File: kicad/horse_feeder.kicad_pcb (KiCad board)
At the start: 2 copper layers, 100 x 80 mm, 81 parts, among them J1 Screw_Terminal_01x04, J10 Conn_01x04_Male, J2 Screw_Terminal_01x04, J3 Screw_Terminal_01x04, J4 Screw_Terminal_01x04, J5 Screw_Terminal_01x04, J6 Screw_Terminal_01x04, J8 Barrel_Jack_Switch_Pin3Ring, J9 Barrel_Jack_Switch_Pin3Ring, Q1 BSS306NH, Q2 BSS306NH, Q3 BSS306NH, Q4 BSS306NH, Q5 BSS306NH, Q6 BSS306NH, SW1 SW_Push, SW2 SW_Push, SW3 SW_Push, SW4 SW_Push, U1 IX4340NE, U2 IX4340NE, U3 IX4340NE, U4 ESP32DevKitCV4, U5 L7809, U6 L7805

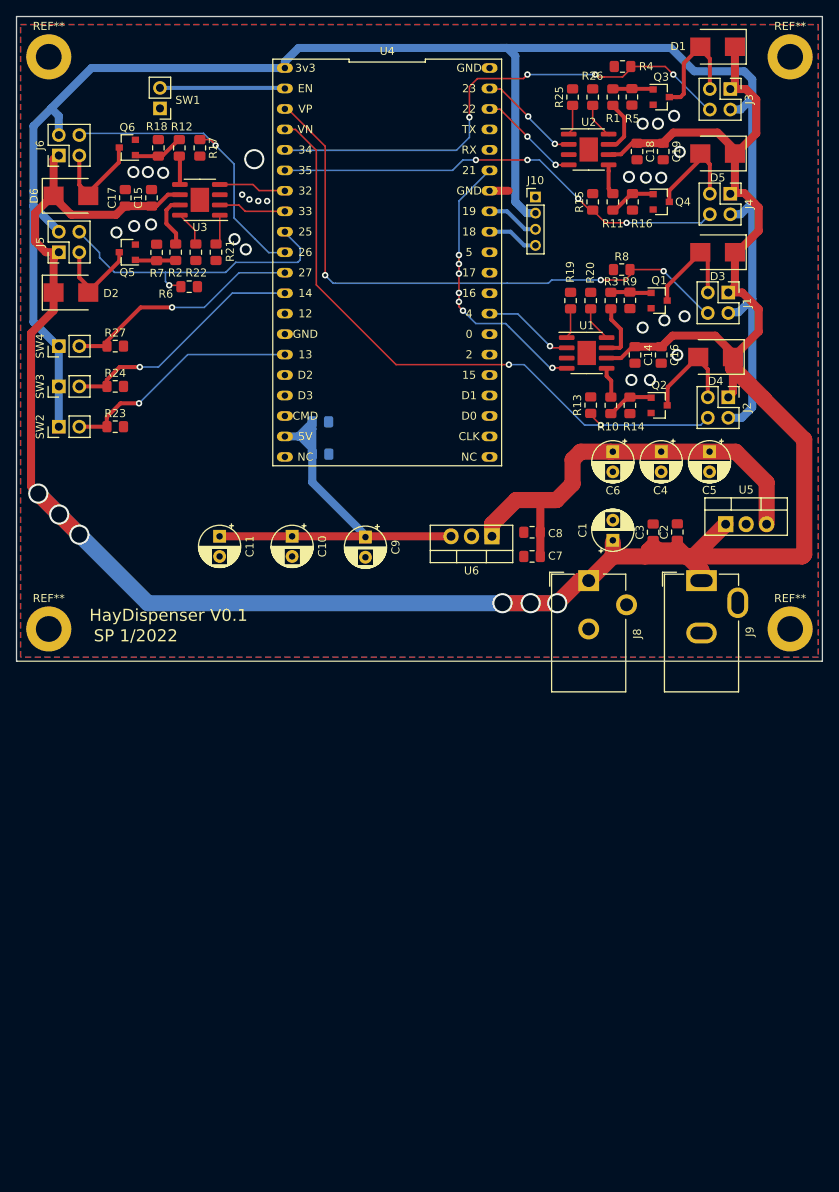
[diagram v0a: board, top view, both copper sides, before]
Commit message: Added pullups for I2C
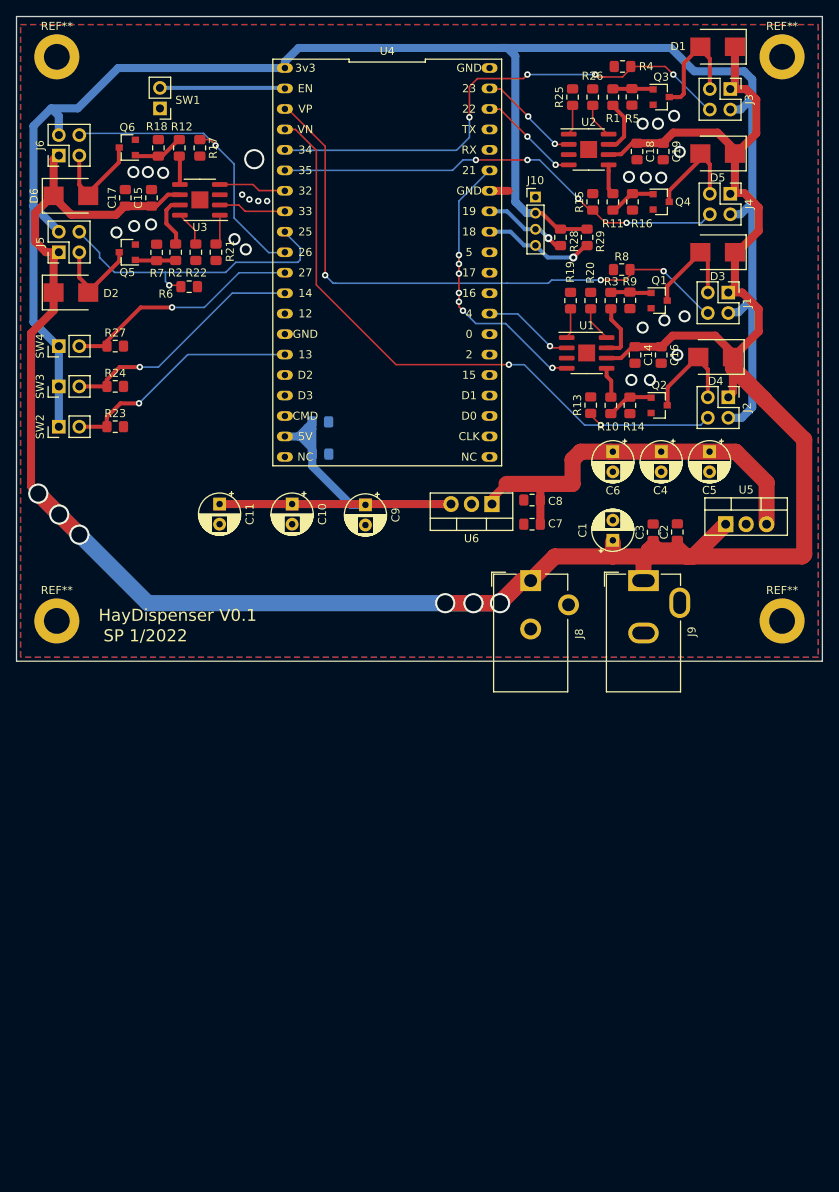
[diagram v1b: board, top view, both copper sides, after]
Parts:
- removed the REF** at (116.0, 45.0)
- removed the REF** at (24.0, 45.0)
- removed the REF** at (24.0, 116.0)
- added R28: 3k3, Resistor_SMD:R_0805_2012Metric_Pad1.15x1.40mm_HandSolder, F.Cu at (87.5, 67.4)
- added R29: 3k3, Resistor_SMD:R_0805_2012Metric_Pad1.15x1.40mm_HandSolder, F.Cu at (90.8, 67.4)
- added REF**: MountingHole_3.2mm_M3_DIN965_Pad, MountingHole:MountingHole_3.2mm_M3_DIN965_Pad, F.Cu at (115.0, 45.0)
- added REF**: MountingHole_3.2mm_M3_DIN965_Pad, MountingHole:MountingHole_3.2mm_M3_DIN965_Pad, F.Cu at (25.0, 45.0)
- added REF**: MountingHole_3.2mm_M3_DIN965_Pad, MountingHole:MountingHole_3.2mm_M3_DIN965_Pad, F.Cu at (25.0, 115.0)
- U1, U2, U3: footprint Package_SO:SOIC-8-1EP_3.9x4.9mm_P1.27mm_EP2.29x3mm -> mosfet_drivers:IX4340NE
- moved J8 7.20 mm to (83.8, 110.0)
- moved J9 7.20 mm to (97.8, 110.0)
- moved C10 4.00 mm to (54.2, 100.5)
- moved C11 4.00 mm to (45.2, 100.5)
- moved C7 4.00 mm to (84.0, 103.0)
- moved C8 4.00 mm to (84.0, 100.0)
- moved C9 4.00 mm to (63.3, 100.6)
- moved U6 4.00 mm to (79.0, 100.5)
- moved REF** 1.41 mm to (115.0, 115.0)
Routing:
- net +12V: track 322.8 -> 334.2 mm
- net /mcu/SCL: track 6.50 -> 14.1 mm, vias 0 -> 1
- net +3V3: track 219.9 -> 227.1 mm
- net /mcu/SDA: track 6.72 -> 10.7 mm, vias 0 -> 1
- net +5V: track 58.2 -> 56.1 mm
- net +9V: track 56.8 -> 58.0 mm

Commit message: KiCAD latest version now up to date
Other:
- net class Default removed
- net class Minimum removed
- net class Power removed
- net class Power2 removed
- net class Signal removed

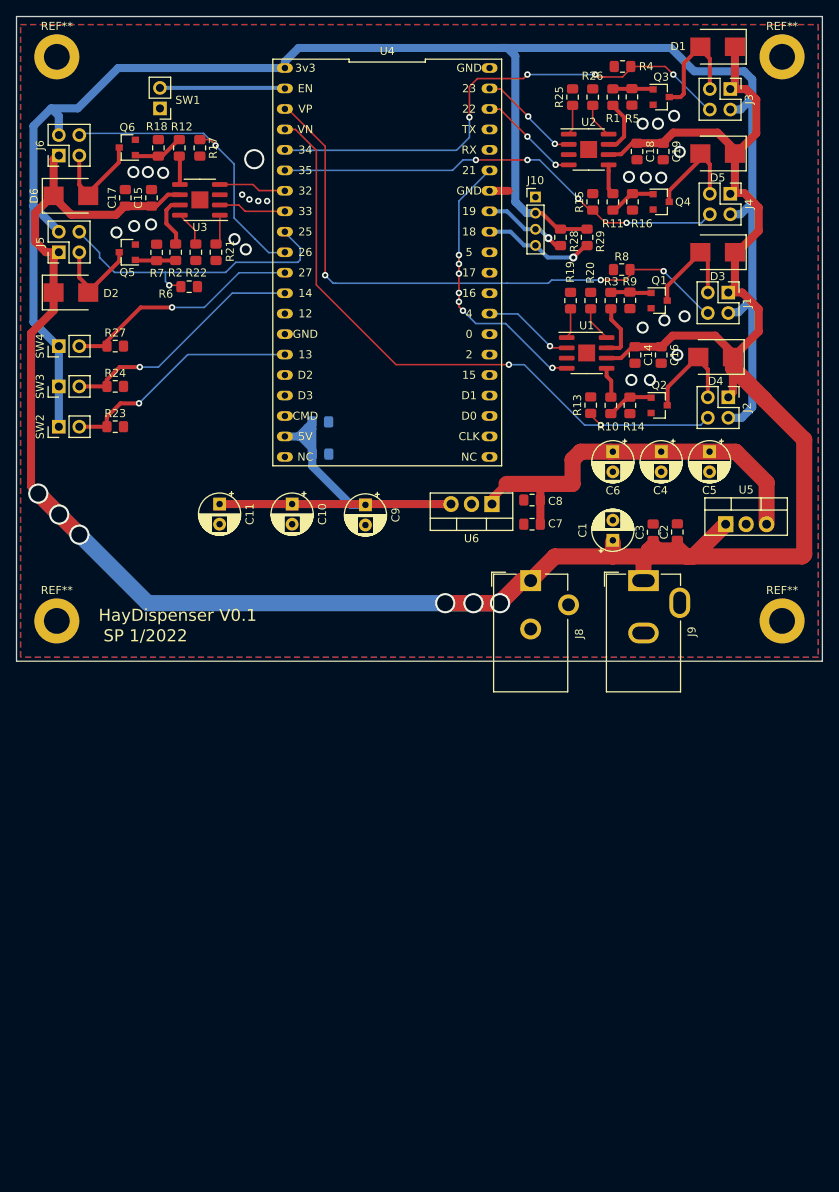
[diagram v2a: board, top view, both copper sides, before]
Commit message: Update PCB with IO expander
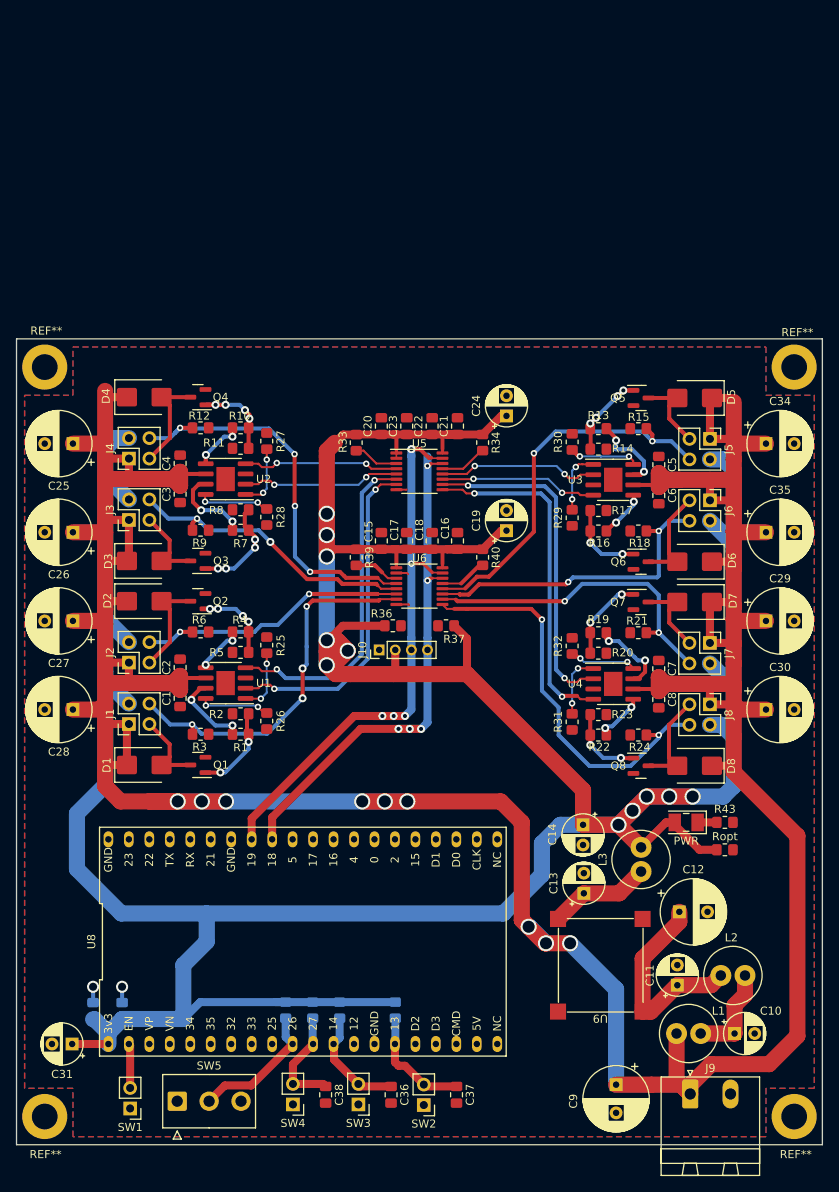
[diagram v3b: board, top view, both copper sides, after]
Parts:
- removed the REF** at (115.0, 115.0)
- removed the REF** at (115.0, 45.0)
- removed the REF** at (25.0, 115.0)
- removed the REF** at (25.0, 45.0)
- added C20: 100p, Capacitor_SMD:C_0805_2012Metric_Pad1.18x1.45mm_HandSolder, F.Cu at (65.3, 90.8)
- added C21: 100p, Capacitor_SMD:C_0805_2012Metric_Pad1.18x1.45mm_HandSolder, F.Cu at (74.7, 90.8)
- added C22: 47n, Capacitor_SMD:C_0805_2012Metric_Pad1.18x1.45mm_HandSolder, F.Cu at (71.6, 90.8)
- added C23: 47n, Capacitor_SMD:C_0805_2012Metric_Pad1.18x1.45mm_HandSolder, F.Cu at (68.4, 90.8)
- added C24: 100u, Capacitor_THT:CP_Radial_D5.0mm_P2.50mm, F.Cu at (80.8, 89.6)
- added C25: 330u, Capacitor_THT:CP_Radial_D8.0mm_P3.50mm, F.Cu at (27.0, 93.0)
- added C26: 330u, Capacitor_THT:CP_Radial_D8.0mm_P3.50mm, F.Cu at (27.0, 104.0)
- added C27: 330u, Capacitor_THT:CP_Radial_D8.0mm_P3.50mm, F.Cu at (27.0, 115.0)
- added C28: 330u, Capacitor_THT:CP_Radial_D8.0mm_P3.50mm, F.Cu at (27.0, 126.0)
- added C29: 330u, Capacitor_THT:CP_Radial_D8.0mm_P3.50mm, F.Cu at (113.0, 115.0)
- added C30: 330u, Capacitor_THT:CP_Radial_D8.0mm_P3.50mm, F.Cu at (113.0, 126.0)
- added C31: 100u, Capacitor_THT:CP_Radial_D5.0mm_P2.50mm, F.Cu at (26.9, 167.5)
- added C32: 47n, Capacitor_SMD:C_0805_2012Metric_Pad1.18x1.45mm_HandSolder, B.Cu at (29.5, 163.4)
- added C33: 100p, Capacitor_SMD:C_0805_2012Metric_Pad1.18x1.45mm_HandSolder, B.Cu at (33.1, 163.4)
- added C34: 330u, Capacitor_THT:CP_Radial_D8.0mm_P3.50mm, F.Cu at (113.0, 93.0)
- added C35: 330u, Capacitor_THT:CP_Radial_D8.0mm_P3.50mm, F.Cu at (113.0, 104.0)
- added C36: 47u, Capacitor_SMD:C_0805_2012Metric_Pad1.18x1.45mm_HandSolder, F.Cu at (66.5, 173.8)
- added C37: 47u, Capacitor_SMD:C_0805_2012Metric_Pad1.18x1.45mm_HandSolder, F.Cu at (74.6, 173.8)
- added C38: 47u, Capacitor_SMD:C_0805_2012Metric_Pad1.18x1.45mm_HandSolder, F.Cu at (58.4, 173.8)
- added D7: US2D, Diode_SMD:D_SMB, F.Cu at (104.1, 112.7)
- added D8: US2D, Diode_SMD:D_SMB, F.Cu at (104.1, 133.0)
- added J7: Screw_Terminal_01x04, Connector_PinHeader_2.54mm:PinHeader_2x02_P2.54mm_Vertical, F.Cu at (106.0, 117.7)
- added L1: 82u, Inductor_THT:L_Radial_D7.0mm_P3.00mm, F.Cu at (101.9, 166.2)
- added L2: 22u, Inductor_THT:L_Radial_D7.0mm_P3.00mm, F.Cu at (110.4, 159.0)
- added L3: 22u, Inductor_THT:L_Radial_D7.0mm_P3.00mm, F.Cu at (97.5, 146.1)
- added PWR: LED, LED_SMD:LED_PLCC-2_3x2mm_KA, F.Cu at (103.1, 140.0)
- added Q7: BSS306NH, Package_TO_SOT_SMD:SOT-23, F.Cu at (97.5, 112.7)
- added Q8: BSS306NH, Package_TO_SOT_SMD:SOT-23, F.Cu at (97.5, 133.0)
- added R30: 0, Resistor_SMD:R_0805_2012Metric_Pad1.20x1.40mm_HandSolder, F.Cu at (89.0, 92.8)
- added R31: 0, Resistor_SMD:R_0805_2012Metric_Pad1.20x1.40mm_HandSolder, F.Cu at (88.9, 127.5)
- added R32: 0, Resistor_SMD:R_0805_2012Metric_Pad1.20x1.40mm_HandSolder, F.Cu at (88.9, 118.1)
- added R33: 3k3, Resistor_SMD:R_0805_2012Metric_Pad1.20x1.40mm_HandSolder, F.Cu at (62.2, 92.9)
- added R34: 3k3, Resistor_SMD:R_0805_2012Metric_Pad1.20x1.40mm_HandSolder, F.Cu at (77.8, 92.9)
- added R35: 10k, Resistor_SMD:R_0805_2012Metric_Pad1.20x1.40mm_HandSolder, B.Cu at (67.0, 163.3)
- added R36: 3k3, Resistor_SMD:R_0805_2012Metric_Pad1.20x1.40mm_HandSolder, F.Cu at (66.7, 115.6)
- added R37: 3k3, Resistor_SMD:R_0805_2012Metric_Pad1.20x1.40mm_HandSolder, F.Cu at (73.3, 115.6)
- added R38: 10k, Resistor_SMD:R_0805_2012Metric_Pad1.20x1.40mm_HandSolder, B.Cu at (60.1, 163.3)
- added R39: 3k3, Resistor_SMD:R_0805_2012Metric_Pad1.20x1.40mm_HandSolder, F.Cu at (62.2, 107.1)
- added R40: 3k3, Resistor_SMD:R_0805_2012Metric_Pad1.20x1.40mm_HandSolder, F.Cu at (77.8, 107.1)
- added R41: 10k, Resistor_SMD:R_0805_2012Metric_Pad1.20x1.40mm_HandSolder, B.Cu at (56.8, 163.3)
- added R42: 3k3, Resistor_SMD:R_0805_2012Metric_Pad1.20x1.40mm_HandSolder, B.Cu at (53.4, 163.3)
- added R43: 68, Resistor_SMD:R_0805_2012Metric_Pad1.20x1.40mm_HandSolder, F.Cu at (107.9, 140.0)
- added REF**: MountingHole_3.2mm_M3_DIN965_Pad, MountingHole:MountingHole_3.2mm_M3_DIN965_Pad, F.Cu at (116.5, 176.5)
- added REF**: MountingHole_3.2mm_M3_DIN965_Pad, MountingHole:MountingHole_3.2mm_M3_DIN965_Pad, F.Cu at (23.5, 83.5)
- added REF**: MountingHole_3.2mm_M3_DIN965_Pad, MountingHole:MountingHole_3.2mm_M3_DIN965_Pad, F.Cu at (116.5, 83.5)
- added REF**: MountingHole_3.2mm_M3_DIN965_Pad, MountingHole:MountingHole_3.2mm_M3_DIN965_Pad, F.Cu at (23.5, 176.5)
- added Ropt: 330, Resistor_SMD:R_0805_2012Metric_Pad1.20x1.40mm_HandSolder, F.Cu at (107.9, 143.4)
- added SW5: SW_SPDT, Connector_TE-Connectivity:TE_826576-3_1x03_P3.96mm_Vertical, F.Cu at (39.9, 174.6)
- added U8: ESP32DevKitCV4, devkits:ESP32_DevkitC_ExtraPins, F.Cu at (54.3, 154.8)
- added U9: ~, devkits:AMSROL-783, F.Cu at (92.4, 158.2)
- C1, C5: value 100u -> 100n; footprint Capacitor_THT:CP_Radial_D5.0mm_P2.50mm -> Capacitor_SMD:C_0805_2012Metric_Pad1.18x1.45mm_HandSolder
- C10: value 47u -> 10u
- C11: value 4.7u -> 10u
- C12: value C -> 330u; footprint Capacitor_SMD:C_0805_2012Metric_Pad1.15x1.40mm_HandSolder -> Capacitor_THT:CP_Radial_D8.0mm_P3.50mm; moved to F.Cu
- C13: value C -> 10u; footprint Capacitor_SMD:C_0805_2012Metric_Pad1.15x1.40mm_HandSolder -> Capacitor_THT:CP_Radial_D5.0mm_P2.50mm; moved to F.Cu
- C14: value 100n -> 10u; footprint Capacitor_SMD:C_0805_2012Metric_Pad1.15x1.40mm_HandSolder -> Capacitor_THT:CP_Radial_D5.0mm_P2.50mm
- C15: value 100n -> 100p; footprint Capacitor_SMD:C_0805_2012Metric_Pad1.15x1.40mm_HandSolder -> Capacitor_SMD:C_0805_2012Metric_Pad1.18x1.45mm_HandSolder
- C16: value 1u -> 100p; footprint Capacitor_SMD:C_0805_2012Metric_Pad1.15x1.40mm_HandSolder -> Capacitor_SMD:C_0805_2012Metric_Pad1.18x1.45mm_HandSolder
- C17: value 1u -> 47n; footprint Capacitor_SMD:C_0805_2012Metric_Pad1.15x1.40mm_HandSolder -> Capacitor_SMD:C_0805_2012Metric_Pad1.18x1.45mm_HandSolder
- C18: value 100n -> 47n; footprint Capacitor_SMD:C_0805_2012Metric_Pad1.15x1.40mm_HandSolder -> Capacitor_SMD:C_0805_2012Metric_Pad1.18x1.45mm_HandSolder
- C19: value 1u -> 100u; footprint Capacitor_SMD:C_0805_2012Metric_Pad1.15x1.40mm_HandSolder -> Capacitor_THT:CP_Radial_D5.0mm_P2.50mm
- C2: value 100n -> 1u; footprint Capacitor_SMD:C_0805_2012Metric_Pad1.15x1.40mm_HandSolder -> Capacitor_SMD:C_0805_2012Metric_Pad1.18x1.45mm_HandSolder
- C3: value 100p -> 100n; footprint Capacitor_SMD:C_0805_2012Metric_Pad1.15x1.40mm_HandSolder -> Capacitor_SMD:C_0805_2012Metric_Pad1.18x1.45mm_HandSolder
- C4, C6: value 100u -> 1u; footprint Capacitor_THT:CP_Radial_D5.0mm_P2.50mm -> Capacitor_SMD:C_0805_2012Metric_Pad1.18x1.45mm_HandSolder
- C7: footprint Capacitor_SMD:C_0805_2012Metric_Pad1.15x1.40mm_HandSolder -> Capacitor_SMD:C_0805_2012Metric_Pad1.18x1.45mm_HandSolder
- C8: value 4.7u -> 1u; footprint Capacitor_SMD:C_0805_2012Metric_Pad1.15x1.40mm_HandSolder -> Capacitor_SMD:C_0805_2012Metric_Pad1.18x1.45mm_HandSolder
- C9: value 100u -> 330u; footprint Capacitor_THT:CP_Radial_D5.0mm_P2.50mm -> Capacitor_THT:CP_Radial_D8.0mm_P3.50mm
- J10: value Conn_01x04_Male -> Conn_01x04_Pin
- J8: value Barrel_Jack_Switch_Pin3Ring -> Screw_Terminal_01x04; footprint Connector_BarrelJack:BarrelJack_CUI_PJ-102AH_Horizontal -> Connector_PinHeader_2.54mm:PinHeader_2x02_P2.54mm_Vertical
- J9: value Barrel_Jack_Switch_Pin3Ring -> Screw_Terminal_01x02; footprint connectors:BarrelJack_CUI_PJ-102AH_Horizontal -> Connector_Phoenix_MSTB:PhoenixContact_MSTBA_2,5_2-G_1x02_P5.00mm_Horizontal
- R1, R10, R14, R17, R19, R22, R23, R25, R26, R5, R8: footprint Resistor_SMD:R_0805_2012Metric_Pad1.15x1.40mm_HandSolder -> Resistor_SMD:R_0805_2012Metric_Pad1.20x1.40mm_HandSolder
- R11, R2, R20: value 0 -> 10k; footprint Resistor_SMD:R_0805_2012Metric_Pad1.15x1.40mm_HandSolder -> Resistor_SMD:R_0805_2012Metric_Pad1.20x1.40mm_HandSolder
- R12, R21, R3: value 0 -> 3k3; footprint Resistor_SMD:R_0805_2012Metric_Pad1.15x1.40mm_HandSolder -> Resistor_SMD:R_0805_2012Metric_Pad1.20x1.40mm_HandSolder
- R13, R16, R27, R4, R7: value 10k -> 0; footprint Resistor_SMD:R_0805_2012Metric_Pad1.15x1.40mm_HandSolder -> Resistor_SMD:R_0805_2012Metric_Pad1.20x1.40mm_HandSolder
- R15, R18, R24, R6, R9: value 10k -> 3k3; footprint Resistor_SMD:R_0805_2012Metric_Pad1.15x1.40mm_HandSolder -> Resistor_SMD:R_0805_2012Metric_Pad1.20x1.40mm_HandSolder
- R28, R29: value 3k3 -> 0; footprint Resistor_SMD:R_0805_2012Metric_Pad1.15x1.40mm_HandSolder -> Resistor_SMD:R_0805_2012Metric_Pad1.20x1.40mm_HandSolder
- U1, U2, U3: footprint mosfet_drivers:IX4340NE -> Package_SO:SOIC-8-1EP_3.9x4.9mm_P1.27mm_EP2.29x3mm
- U4: value ESP32DevKitCV4 -> IX4340NE; footprint devkits:ESP32_DevkitC_ExtraPins -> Package_SO:SOIC-8-1EP_3.9x4.9mm_P1.27mm_EP2.29x3mm
- U5: value L7809 -> ~; footprint Package_TO_SOT_THT:TO-220-3_Vertical -> Package_SO:TSSOP-16_4.4x5mm_P0.65mm
- U6: value L7805 -> ~; footprint Package_TO_SOT_THT:TO-220-3_Vertical -> Package_SO:TSSOP-16_4.4x5mm_P0.65mm
- moved SW1 124.2 mm to (34.1, 175.5)
- moved D1 114.0 mm to (35.9, 132.9), turned to 0 degrees
- moved SW4 98.5 mm to (54.3, 175.0), turned to 180 degrees
- moved SW3 96.5 mm to (62.4, 175.0), turned to 180 degrees
- moved SW2 95.6 mm to (70.5, 175.1), turned to 180 degrees
- moved J3 91.8 mm to (34.0, 102.5), turned to 90 degrees
- moved J1 91.6 mm to (34.0, 127.8), turned to 90 degrees
- moved R1 91.6 mm to (47.8, 129.1), turned to 180 degrees
- moved J6 91.4 mm to (106.0, 100.0), turned to -90 degrees
- moved D6 89.7 mm to (104.2, 107.7), turned to 180 degrees
- moved R26 87.4 mm to (51.0, 127.4), turned to 90 degrees
- moved C10 85.6 mm to (109.1, 166.2), turned to 0 degrees
- moved R4 84.7 mm to (47.8, 116.4)
- moved R5 84.3 mm to (47.8, 118.9), turned to 180 degrees
- moved J5 84.1 mm to (106.0, 92.4), turned to -90 degrees
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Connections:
- net /IOs/LOCK_EN2 renamed /IOS/LOCK_EN1
- net /IOs/LOCK_EN3 renamed /IOS/LOCK_EN0
- C10 pad 1: +5V -> Net-(C10-Pad1)
- C11 pad 1: +5V -> Net-(U9-VIN)
- C12 pad 1: +5V -> Net-(U9-VIN)
- C13 pad 1: +5V -> Net-(U9-VOUT)
- C14 pad 1: +12V -> +3V3
- C15 pad 1: +12V -> +3V3
- C16 pad 1: +12V -> +3V3
- C17 pad 1: +12V -> +3V3
- C18 pad 1: +12V -> +3V3
- C19 pad 1: +12V -> +3V3
- C4 pad 1: +9V -> +12V
- C5 pad 1: +9V -> +12V
- C6 pad 1: +9V -> +12V
- C7 pad 1: +9V -> +12V
- C8 pad 1: +9V -> +12V
- C9 pad 1: +5V -> +12V
- D1 pad 2: Net-(D1-Pad2) -> Net-(D1-A)
- D2 pad 2: Net-(D2-Pad2) -> Net-(D2-A)
- D3 pad 2: Net-(D3-Pad2) -> Net-(D3-A)
- D4 pad 2: Net-(D4-Pad2) -> Net-(D4-A)
- D5 pad 2: Net-(D5-Pad2) -> Net-(D5-A)
- J1 pad 3: Net-(D3-Pad2) -> Net-(D1-A)
- J1 pad 4: /LOCK_DET0 -> /IOS/LOCK_DET0
- J10 pad 3: /mcu/SDA -> /MCU/SDA
- J10 pad 4: /mcu/SCL -> /MCU/SCL
- J2 pad 3: Net-(D4-Pad2) -> Net-(D2-A)
- J2 pad 4: /LOCK_DET1 -> /IOS/LOCK_DET1
- J3 pad 3: Net-(D1-Pad2) -> Net-(D3-A)
- J3 pad 4: /LOCK_DET2 -> /IOS/LOCK_DET2
- J4 pad 3: Net-(D5-Pad2) -> Net-(D4-A)
- J4 pad 4: /LOCK_DET3 -> /IOS/LOCK_DET3
- J5 pad 3: Net-(D2-Pad2) -> Net-(D5-A)
- J5 pad 4: /LOCK_DET4 -> /IOS/LOCK_DET4
- J6 pad 4: /LOCK_DET5 -> /IOS/LOCK_DET5
- J8 pad 2: GND -> +3V3
- J8 pad 3: GND -> Net-(D8-A)
- Q1 pad 1: Net-(Q1-Pad1) -> Net-(Q1-G)
- Q1 pad 3: Net-(D3-Pad2) -> Net-(D1-A)
- Q2 pad 1: Net-(Q2-Pad1) -> Net-(Q2-G)
- Q2 pad 3: Net-(D4-Pad2) -> Net-(D2-A)
- Q3 pad 1: Net-(Q3-Pad1) -> Net-(Q3-G)
- Q3 pad 3: Net-(D1-Pad2) -> Net-(D3-A)
- Q4 pad 1: Net-(Q4-Pad1) -> Net-(Q4-G)
- Q4 pad 3: Net-(D5-Pad2) -> Net-(D4-A)
- Q5 pad 1: Net-(Q5-Pad1) -> Net-(Q5-G)
- Q5 pad 3: Net-(D2-Pad2) -> Net-(D5-A)
- Q6 pad 1: Net-(Q6-Pad1) -> Net-(Q6-G)
- R1 pad 1: Net-(Q3-Pad1) -> Net-(Q1-G)
- R1 pad 2: /IOs/LOCK2 -> /IOS/LOCK0
- R10 pad 1: Net-(Q2-Pad1) -> Net-(Q4-G)
- R10 pad 2: /IOs/LOCK1 -> /IOS/LOCK3
- R11 pad 1: Net-(Q4-Pad1) -> Net-(Q4-G)
- R11 pad 2: /IOs/LOCK3 -> GND
- R12 pad 1: Net-(Q6-Pad1) -> /IOS/LOCK_DET3
- R12 pad 2: /IOs/LOCK5 -> GND
- R13 pad 1: /LOCK_DET1 -> Net-(Q5-G)
- R13 pad 2: GND -> /IOS/LOCK4
- R14 pad 1: Net-(Q2-Pad1) -> Net-(Q5-G)
- R15 pad 1: /LOCK_DET3 -> /IOS/LOCK_DET4
- R16 pad 1: Net-(Q4-Pad1) -> Net-(Q6-G)
- R16 pad 2: GND -> /IOS/LOCK5
- R17 pad 1: /LOCK_DET5 -> Net-(Q6-G)
- R18 pad 1: Net-(Q6-Pad1) -> /IOS/LOCK_DET5
- R19 pad 1: Net-(R19-Pad1) -> Net-(Q7-G)
- R19 pad 2: /IOs/LOCK_EN0 -> /IOS/LOCK6
- R2 pad 1: Net-(Q5-Pad1) -> Net-(Q1-G)
- R2 pad 2: /IOs/LOCK4 -> GND
- R20 pad 1: /IOs/LOCK_EN1 -> Net-(Q7-G)
- R20 pad 2: Net-(R20-Pad2) -> GND
- R21 pad 1: Net-(R21-Pad1) -> /IOS/LOCK_DET6
- R21 pad 2: /IOs/LOCK_EN4 -> GND
- R22 pad 1: /IOs/LOCK_EN5 -> Net-(Q8-G)
- R22 pad 2: Net-(R22-Pad2) -> /IOS/LOCK7
- R23 pad 1: /SELECT -> Net-(Q8-G)
- R24 pad 1: /RIGHT -> /IOS/LOCK_DET7
- R25 pad 1: Net-(R25-Pad1) -> Net-(U1-ENA)
- R26 pad 2: Net-(R26-Pad2) -> Net-(U1-ENB)
- R27 pad 1: /LEFT -> Net-(U2-ENA)
- R27 pad 2: GND -> /IOS/LOCK_EN3
- R28 pad 1: +3V3 -> /IOS/LOCK_EN2
- R28 pad 2: /mcu/SDA -> Net-(U2-ENB)
- R29 pad 1: +3V3 -> Net-(U3-ENA)
- R29 pad 2: /mcu/SCL -> /IOS/LOCK_EN5
- R3 pad 1: Net-(Q1-Pad1) -> /IOS/LOCK_DET0
- R3 pad 2: /IOs/LOCK0 -> GND
- R4 pad 1: /LOCK_DET2 -> Net-(Q2-G)
- R4 pad 2: GND -> /IOS/LOCK1
- R5 pad 1: Net-(Q3-Pad1) -> Net-(Q2-G)
- R6 pad 1: /LOCK_DET4 -> /IOS/LOCK_DET1
- R7 pad 1: Net-(Q5-Pad1) -> Net-(Q3-G)
- R7 pad 2: GND -> /IOS/LOCK2
- R8 pad 1: /LOCK_DET0 -> Net-(Q3-G)
- R9 pad 1: Net-(Q1-Pad1) -> /IOS/LOCK_DET2
- SW1 pad 2: Net-(SW1-Pad2) -> Net-(U8-EN)
- SW2 pad 1: +3V3 -> GND
- SW2 pad 2: /SELECT -> /MCU/SELECT
- SW3 pad 1: +3V3 -> GND
- SW3 pad 2: /RIGHT -> /MCU/RIGHT
- SW4 pad 1: +3V3 -> GND
- SW4 pad 2: /LEFT -> /MCU/LEFT
- U1 pad 1: Net-(R19-Pad1) -> Net-(U1-ENA)
- U1 pad 2: /mcu/LOCK0 -> /IOS/LOCK_IN0
- U1 pad 4: /mcu/LOCK1 -> /IOS/LOCK_IN1
- U1 pad 5: /IOs/LOCK1 -> /IOS/LOCK1
- U1 pad 7: /IOs/LOCK0 -> /IOS/LOCK0
- U1 pad 8: Net-(R20-Pad2) -> Net-(U1-ENB)
- U2 pad 1: Net-(R25-Pad1) -> Net-(U2-ENA)
- U2 pad 2: /mcu/LOCK2 -> /IOS/LOCK_IN2
- U2 pad 4: /mcu/LOCK3 -> /IOS/LOCK_IN3
- U2 pad 5: /IOs/LOCK3 -> /IOS/LOCK3
- U2 pad 7: /IOs/LOCK2 -> /IOS/LOCK2
- U2 pad 8: Net-(R26-Pad2) -> Net-(U2-ENB)
- U3 pad 1: Net-(R21-Pad1) -> Net-(U3-ENA)
- U3 pad 2: /mcu/LOCK4 -> /IOS/LOCK_IN4
- U3 pad 4: /mcu/LOCK5 -> /IOS/LOCK_IN5
- U3 pad 5: /IOs/LOCK5 -> /IOS/LOCK5
- U3 pad 7: /IOs/LOCK4 -> /IOS/LOCK4
- U3 pad 8: Net-(R22-Pad2) -> Net-(U3-ENB)
- U4 pad 1: +3V3 -> Net-(U4-ENA)
- U4 pad 2: Net-(SW1-Pad2) -> /IOS/LOCK_IN6
- U4 pad 3: /LOCK_DET0 -> GND
- U4 pad 4: /LOCK_DET1 -> /IOS/LOCK_IN7
- U4 pad 5: /LOCK_DET2 -> /IOS/LOCK7
- U4 pad 6: /LOCK_DET3 -> +12V
- U4 pad 7: /mcu/LOCK5 -> /IOS/LOCK6
- U4 pad 8: /mcu/LOCK4 -> Net-(U4-ENB)
- U4 pad 9: /LOCK_DET4 -> (no net)
- U5 pad 1: +12V -> +3V3
- U5 pad 2: GND -> +3V3
- U5 pad 3: +9V -> Net-(U5-~RESET)
- U6 pad 1: +9V -> +3V3
- U6 pad 3: +5V -> Net-(U6-~RESET)
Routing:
- net +3V3: track 227.1 -> 487.5 mm, vias 0 -> 11
- net +12V: track 334.2 -> 464.3 mm, vias 6 -> 9
- net /LOCK_DET1: track 79.8 -> 0.00 mm, vias 2 -> 0
- net /LOCK_DET0: track 74.1 -> 0.00 mm, vias 3 -> 0
- net /MCU/SDA: track 0.00 -> 72.8 mm, vias 0 -> 5
- net /MCU/SCL: track 0.00 -> 66.7 mm, vias 0 -> 5
- net /LOCK_DET2: track 63.4 -> 0.00 mm, vias 4 -> 0
- net +9V: track 58.0 -> 0.00 mm
- net /LOCK_DET3: track 57.1 -> 0.00 mm, vias 4 -> 0
- net +5V: track 56.1 -> 0.00 mm
- net /IOS/LOCK_DET7: track 0.00 -> 50.0 mm, vias 0 -> 2
- net /IOS/LOCK_DET3: track 0.00 -> 49.0 mm, vias 0 -> 4
- net /IOS/LOCK_DET4: track 0.00 -> 47.7 mm, vias 0 -> 2
- net /IOS/LOCK_DET0: track 0.00 -> 46.7 mm, vias 0 -> 4
- net /IOS/LOCK_IN7: track 0.00 -> 42.8 mm, vias 0 -> 2
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- added copper zone on B.Cu, net (none)
- removed copper zone on B.Cu, net GND
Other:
- board size 100 x 80 mm -> 100 x 100 mm
- board text removed: "HayDispenser V0.1"
- board text removed: "SP 1/2022"

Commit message: Fix remaining DRC + ERC, ready for manufacturing
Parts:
- added C39: 47u, Capacitor_SMD:C_0805_2012Metric_Pad1.18x1.45mm_HandSolder, F.Cu at (66.0, 118.6)
- moved J10 5.40 mm to (65.0, 124.0)
- moved R36 1.00 mm to (65.7, 115.6)
- moved R37 1.00 mm to (74.3, 115.6)
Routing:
- net /MCU/SCL: track 66.7 -> 68.8 mm, vias 5 -> 6
- net /MCU/SDA: track 72.8 -> 75.0 mm, vias 5 -> 6
- net +3V3: track 487.5 -> 488.6 mm
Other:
- board text added: "Designed by SP"
- board text added: "HayDispenser Rev 1.2"
- board text added: "VIOLA ON MAAILMAN PARAS PONI!"
